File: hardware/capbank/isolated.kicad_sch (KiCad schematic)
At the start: 10 parts, among them U3 MCP1525-TO, U4 MCP4921-EP

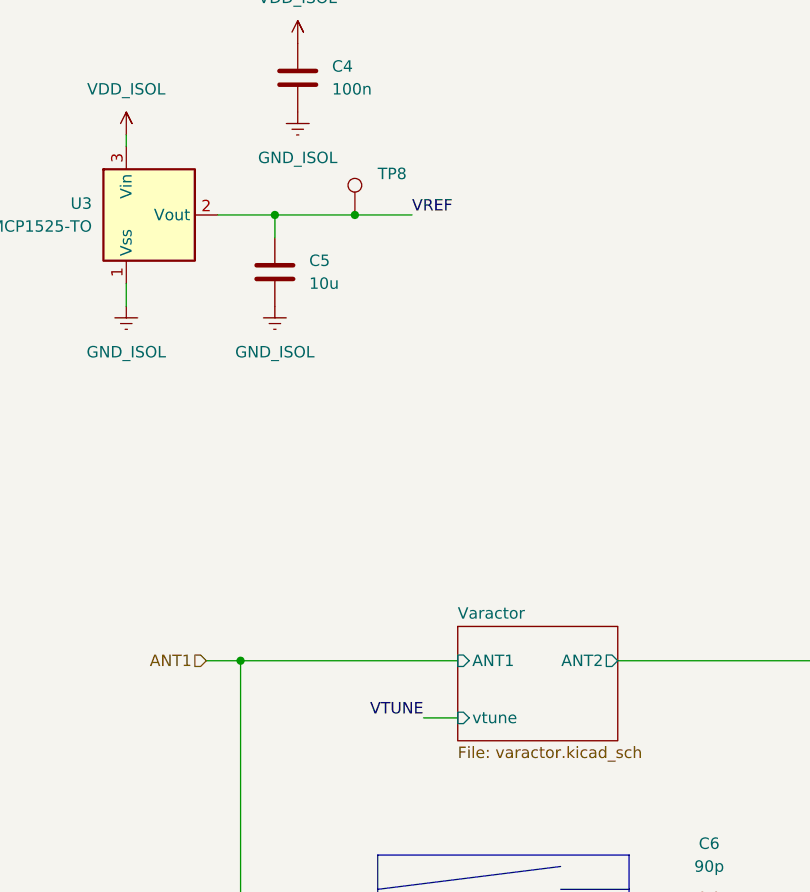
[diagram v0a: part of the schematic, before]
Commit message: Progress, layout nearly completed, build oscillator on breadboard
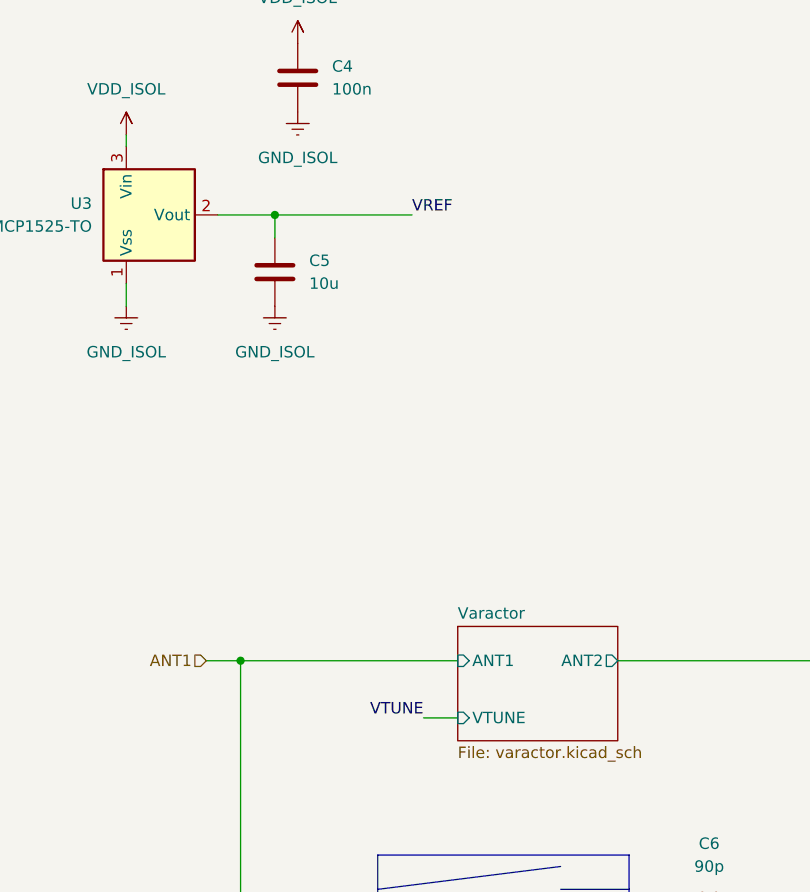
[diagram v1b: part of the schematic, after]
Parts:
- removed TP8: ~, TestPoint:TestPoint_THTPad_1.5x1.5mm_Drill0.7mm, symbol Connector:TestPoint
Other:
- sheet Varactor ports: added VTUNE; removed vtune
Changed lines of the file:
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@@
-	)
-	(junction
-		(at 113.03 66.04)
-		(diameter 0)
-		(color 0 0 0 0)
 	)
 	(junction
@@
 	(wire
 		(pts
-			(xy 113.03 66.04) (xy 119.38 66.04)
-		)
-		(stroke
-			(width 0)
-			(type default)
-		)
-	)
-	(wire
-		(pts
-			(xy 104.14 66.04) (xy 113.03 66.04)
+			(xy 104.14 66.04) (xy 119.38 66.04)
 		)
 		(stroke
@@
 	)
 	(symbol
-		(lib_id "Connector:TestPoint")
-		(at 113.03 66.04 0)
-		(unit 1)
-		(exclude_from_sim no)
-		(in_bom yes)
-		(on_board yes)
-		(dnp no)
-		(fields_autoplaced yes)
-		(property "Reference" "TP8"
-			(at 115.57 61.4679 0)
-			(effects
-				(font
-					(size 1.27 1.27)
-				)
-				(justify left)
-			)
-		)
-		(property "Value" "~"
-			(at 115.57 64.0079 0)
-			(effects
-				(font
-					(size 1.27 1.27)
-				)
-				(justify left)
-			)
-		)
-		(property "Footprint" "TestPoint:TestPoint_THTPad_1.5x1.5mm_Drill0.7mm"
-			(at 118.11 66.04 0)
-			(effects
-				(font
-					(size 1.27 1.27)
-				)
-				(hide yes)
-			)
-		)
-		(property "Datasheet" "~"
-			(at 118.11 66.04 0)
-			(effects
-				(font
-					(size 1.27 1.27)
-				)
-				(hide yes)
-			)
-		)
-		(property "Description" "test point"
-			(at 113.03 66.04 0)
-			(effects
-				(font
-					(size 1.27 1.27)
-				)
-				(hide yes)
-			)
-		)
-		(pin "1"
-		)
-		(instances
-			(project "capbank1"
-				(path "/461cb8a1-2d60-44a8-88b5-d61a3ba14a84/a75e6ab6-702b-4065-b99f-956a48aaae0a"
-					(reference "TP8")
-					(unit 1)
-				)
-			)
-		)
-	)
-	(symbol
 		(lib_id "proj_power:VDD_ISOL")
 		(at 106.68 46.99 0)
@@
 			)
 		)
-		(pin "vtune" input
+		(pin "VTUNE" input
 			(at 124.46 121.92 180)
 			(effects
